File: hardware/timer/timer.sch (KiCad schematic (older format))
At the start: 28 parts, among them J1 Conn_01x24_Male, J2 Conn_01x02_Male, J3 Conn_01x24_Male

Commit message: Recreate timer module with single PCB, clean up libraries
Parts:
- removed D1, D10, D11, D12, D2, D3, D4, D5, D8, D9: LED, LED_THT:LED_D5.0mm, symbol Device:LED
- removed J1, J3: Conn_01x24_Male, Connector_PinHeader_2.54mm:PinHeader_1x24_P2.54mm_Vertical, symbol Connector:Conn_01x24_Male
- removed J2: Conn_01x02_Male, Connector_PinHeader_2.54mm:PinHeader_1x02_P2.54mm_Vertical, symbol Connector:Conn_01x02_Male
- removed R1, R10, R11, R13, R14, R15, R16, R2, R5, R7, R8, R9: R, Resistor_THT:R_Axial_DIN0309_L9.0mm_D3.2mm_P12.70mm_Horizontal, symbol Device:R
- added C1: 0.1uF, Capacitor_SMD:C_0603_1608Metric_Pad1.05x0.95mm_HandSolder, symbol Device:C_Small
- added J2: Conn_01x03_Female, Connector_PinSocket_2.54mm:PinSocket_1x03_P2.54mm_Vertical, symbol Connector:Conn_01x03_Female
- added R5, R6, R7, R8, R9: 100, Resistor_SMD:R_0603_1608Metric_Pad1.05x0.95mm_HandSolder, symbol Device:R_Small
- added U2: HT16K33, Package_SO:SOIC-28W_7.5x17.9mm_P1.27mm, symbol ProjectChips:HT16K33
- D1: renamed from D7; footprint 8402BS:8042BS -> ProjectDisplays:8042BS; symbol large7segment:8402BS -> ProjectDisplays:8402BS
- R3, R4: value R -> 4K7; footprint Resistor_THT:R_Axial_DIN0309_L9.0mm_D3.2mm_P12.70mm_Horizontal -> Resistor_SMD:R_0603_1608Metric_Pad1.05x0.95mm_HandSolder
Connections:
- net at D1.1 (E): now also U2.9 (COM7)
- net at D1.10 (DIG3A): now also R7.1
- net at D1.11 (DIG2A): now also R6.1
- net at D1.12 (F): now also U2.3 (COM1/KS0)
- net at D1.13 (A): now also U2.2 (COM0/AD0)
- net at D1.14 (DIG1A): now also R5.1
- net at D1.2 (D): now also U2.8 (COM6)
- net at D1.3 (DP): now also D1.8 (COLONC), U2.7 (COM5)
- net at D1.4 (C): now also U2.6 (COM4)
- net at D1.5 (G): now also U2.5 (COM3/KS2)
- net at D1.6 (DIG4A): now also R8.1
- net at D1.7 (COLONA): now also R9.1
- net at D1.9 (B): now also U2.4 (COM2/KS1)
- net A4_SDA: now reaches R3.1
- net A4_SDA: now also U2.27 (SDA)
- net A5_SCL: now reaches R4.1
- net A5_SCL: now also U2.26 (SCL)
- net VCC: now reaches R3.2, R4.2
- net VCC: now also C1.2, J2.2 (Pin_2), U2.28 (VDD)
- new net: R9.2, U2.21 (ROW4/K2)
- new net: R8.2, U2.22 (ROW3/K1)
- new net: R7.2, U2.23 (ROW2/A0)
- new net: R6.2, U2.24 (ROW1/A1)
- new net: R5.2, U2.25 (ROW0/A2)
- new net A0: J2.3 (Pin_3)
- new net A1: J2.1 (Pin_1)
- new net GND: C1.1, U2.1 (VSS)
- no-connect marks 0 -> 11
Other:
- moved on the sheet: D1

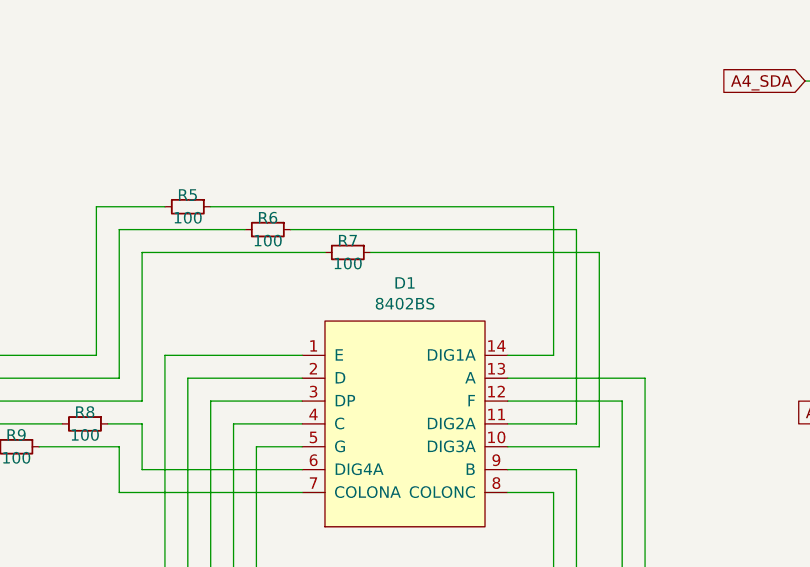
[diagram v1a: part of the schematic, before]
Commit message: Timer PCB: use non-LED RJ45, update layout, reroute
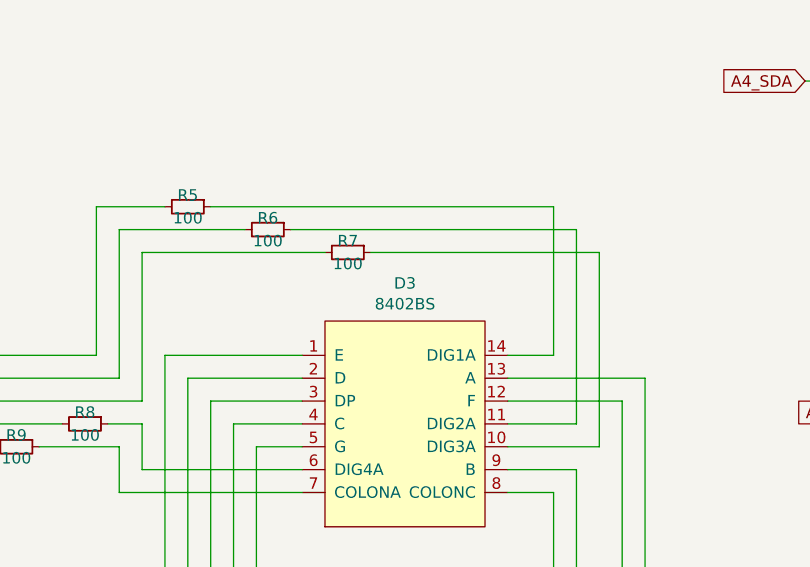
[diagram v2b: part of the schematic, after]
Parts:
- D3: renamed from D1; footprint ProjectDisplays:8042BS -> ProjectDisplays:8402BS
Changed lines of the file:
@@
 $EndDescr
 $Comp
-L ProjectDisplays:8402BS D1
+L ProjectDisplays:8402BS D3
 U 1 1 5DE48E9B
 P 6600 2500
-F 0 "D1" H 6600 2615 50  0000 C CNN
+F 0 "D3" H 6600 2615 50  0000 C CNN
 F 1 "8402BS" H 6600 2524 50  0000 C CNN
-F 2 "ProjectDisplays:8042BS" V 6050 1950 50  0001 C CNN
+F 2 "ProjectDisplays:8402BS" V 6050 1950 50  0001 C CNN
 F 3 "" V 6050 1950 50  0001 C CNN
 	1    6600 2500
@@
 $EndComp
 $Comp
-L power:VCC #PWR?
+L power:VCC #PWR0104
 U 1 1 5EC98D35
 P 8500 2150
-AR Path="/5EC98D35" Ref="#PWR?"  Part="1"
+AR Path="/5EC98D35" Ref="#PWR0104"  Part="1"
 AR Path="/5EF969E2/5EC98D35" Ref="#PWR?"  Part="1"
 AR Path="/5EAC2475/5EC98D35" Ref="#PWR?"  Part="1"
-F 0 "#PWR?" H 8500 2000 50  0001 C CNN
+F 0 "#PWR0104" H 8500 2000 50  0001 C CNN
 F 1 "VCC" H 8518 2323 50  0000 C CNN
 F 2 "" H 8500 2150 50  0001 C CNN
@@
 $EndComp
 $Comp
-L power:VCC #PWR?
+L power:VCC #PWR0105
 U 1 1 5EC98D3B
 P 8850 2150
-AR Path="/5EC98D3B" Ref="#PWR?"  Part="1"
+AR Path="/5EC98D3B" Ref="#PWR0105"  Part="1"
 AR Path="/5EF969E2/5EC98D3B" Ref="#PWR?"  Part="1"
 AR Path="/5EAC2475/5EC98D3B" Ref="#PWR?"  Part="1"
-F 0 "#PWR?" H 8850 2000 50  0001 C CNN
+F 0 "#PWR0105" H 8850 2000 50  0001 C CNN
 F 1 "VCC" H 8868 2323 50  0000 C CNN
 F 2 "" H 8850 2150 50  0001 C CNN
